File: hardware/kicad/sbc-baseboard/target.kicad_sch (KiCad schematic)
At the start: 59 parts, among them J11 Relay COM/NO/NC, J12 Relay COM/NO/NC, J13 Console VREF/TXD/RXD/GND, J14 +5V_TGT out, J15 GPIO + I2C breakout, J18 PSU in (isolated), J19 PSU out (isolated), K701 G6K-2F-Y DC5, K702 G6K-2F-Y DC5, K703 JW1FSN-DC5V, Q701 2N7002, Q702 2N7002, Q703 AO3400A, U701 TXB0104PW, U702 TXB0108PW, U703 TXS0102DCU, U704 TPS26630RGE, U705 LTV-817

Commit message: Re-lay out every sheet around its main component
Nets fan out of each hub IC as wires at pin pitch; connectors, series
parts, pull-ups and power symbols sit at the lane ends, and labels are
kept for nets that leave the page. Supply pins share a bus with their
decoupling; ESD arrays sit on the connector's D-/D+ rows and port
switches on the VBUS row, so every wire into a receptacle is straight;
the stacked USB-A is a two-unit symbol, one per port. Relays move to
their own sheet (8xx). ESD diodes use KiCad's PESD5V0S1UL in SOD-882.

Generator: gen/fanout.py (lane engine), gen/check_geom.py (endpoint
contacts), gen/netcheck.py (wire-level rail merges). ERC, both checks
and a renumbering-tolerant netlist diff against the first pass all
clean; 331 parts, 354 nets.

Co-Authored-By: Claude Fable 5.1 <noreply@anthropic.com>
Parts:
- removed D701, D702: PESD5V0S1UL, Diode_SMD:D_SOD-523, symbol Device:D_TVS
- removed D703, D705, D708, D710: 1N4148W, Diode_SMD:D_SOD-123, symbol Diode:1N4148W
- removed D704, D706, D709: LED RED, LED_SMD:LED_0603_1608Metric, symbol Device:LED
- removed D707: LED GREEN, LED_SMD:LED_0603_1608Metric, symbol Device:LED
- removed J11, J12: Relay COM/NO/NC, Connector_Phoenix_MC:PhoenixContact_MC_1,5_3-G-3.5_1x03_P3.50mm_Horizontal, symbol Connector_Generic:Conn_01x03
- removed J18: PSU in (isolated), Connector_Phoenix_MSTB:PhoenixContact_MSTBA_2,5_2-G-5,08_1x02_P5.08mm_Horizontal, symbol Connector_Generic:Conn_01x02
- removed J19: PSU out (isolated), Connector_Phoenix_MSTB:PhoenixContact_MSTBA_2,5_2-G-5,08_1x02_P5.08mm_Horizontal, symbol Connector_Generic:Conn_01x02
- removed K701, K702: G6K-2F-Y DC5, Relay_SMD:Relay_DPDT_Omron_G6K-2F-Y, symbol Relay:G6K-2
- removed K703: JW1FSN-DC5V, Relay_THT:Relay_SPDT_Panasonic_JW1_FormC, symbol sbcbb:JW1FSN
- removed Q701, Q702: 2N7002, Package_TO_SOT_SMD:SOT-23, symbol Transistor_FET:2N7002
- removed Q703: AO3400A, Package_TO_SOT_SMD:SOT-23, symbol Transistor_FET:AO3400A
- removed R709: 75k, Resistor_SMD:R_0603_1608Metric, symbol Device:R
- removed R710: 3.65k 1%, Resistor_SMD:R_0603_1608Metric, symbol Device:R
- removed R711, R712, R720: 10k, Resistor_SMD:R_0603_1608Metric, symbol Device:R
- removed R713: 20k, Resistor_SMD:R_0603_1608Metric, symbol Device:R
- removed R714, R716: 1k, Resistor_SMD:R_0603_1608Metric, symbol Device:R
- removed R715: 2.2k, Resistor_SMD:R_0603_1608Metric, symbol Device:R
- removed R717: 100k, Resistor_SMD:R_0603_1608Metric, symbol Device:R
- removed R718, R719: 1.8k, Resistor_SMD:R_1206_3216Metric, symbol Device:R
- removed U705: LTV-817, Package_DIP:DIP-4_W7.62mm, symbol Isolator:LTV-817
- added C712: 10n, Capacitor_SMD:C_0603_1608Metric, symbol Device:C
- added D701, D702: PESD5V0S1UL, Diode_SMD:D_SOD-882, symbol Diode:PESD5V0S1UL
- added D703: LED GREEN, LED_SMD:LED_0603_1608Metric, symbol Device:LED
- C707: value 10n -> 100n
- C708: value 1n -> 100n
- C710: value 100n -> 22u; footprint Capacitor_SMD:C_0603_1608Metric -> Capacitor_SMD:C_1206_3216Metric
- C711: value 22u -> 1n; footprint Capacitor_SMD:C_1206_3216Metric -> Capacitor_SMD:C_0603_1608Metric
- R702: value 2.2k -> 75k
- R703: value 1k -> 196k
- R704: value 100k -> 10k
- R705: value 2.2k -> 1k
- R706: value 1k -> 10k
- R707: value 100k -> 20k
- R708: value 196k -> 3.65k 1%
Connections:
- net RLY2_DRV is gone; now on net +3V3: R706.1
- net +3V3: now also C703.2, C705.2, C707.2, R704.1; no longer C702.1, C704.1, C706.1
- net +5V_TGT: now also C708.1, R703.2; no longer C710.1, R708.1
- net GND: now also C702.1, C703.1, C704.1, C705.1, C706.1, C707.1, R702.2, R708.2, C712.2, D701.2 (A), D702.2 (A), D703.1 (K); no longer C702.2, C703.2, C704.2, C705.2, C706.2, C707.2, R704.2
- net TGT_EN: now also R704.2
- net TGT_FAULT_N: now also R706.2
- net TGT_IMON: now also C711.1, R707.1; no longer C708.1
- net VREF_TGT: now also C702.2, C704.2, C706.2; no longer C703.1, C705.1
- net at R705.2: now also D703.2 (A)
- net +5V_PORTS: no longer names the net of R705.1
- net +5V_PORTS: now also C710.1, J14.1 (Pin_1), U704.17 (OUT), U704.18 (OUT); no longer R702.1
- removed net +5V_TGT_OUT: C711.1, J14.1 (Pin_1), U704.17 (OUT), U704.18 (OUT)
- net J13_RXD: no longer names the net of J13.3 (Pin_3), U701.3 (A2)
- net J13_RXD: now also D702.1 (K)
- net J13_TXD: no longer names the net of J13.2 (Pin_2), U701.2 (A1)
- net J13_TXD: now also D701.1 (K)
- net RLY1_DRV: no longer names the net of R703.1
- net RLY1_DRV: now also R702.1, U704.6 (UVLO)
- removed net RLY1_GATE: R703.2, R704.1
- removed net RLY2_GATE: R706.2, R707.1
- net TGT_DVDT: no longer names the net of U704.9 (dVdT)
- net TGT_DVDT: now also C712.1; no longer C707.1
- net TGT_ILIM: no longer names the net of U704.10 (ILIM)
- net TGT_ILIM: now also R708.1
- removed net TGT_UVLO: R708.2, U704.6 (UVLO)
- no-connect marks 26 -> 19
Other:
- note added: "TPS26630: ILIM 3.65k -> ~5 A, UVLO 196k/75k -> 4.3 V, OVP/MODE/PGTH to GND (latch-off). IMON 20k -> 2.8 V at 5 A into PTB2."
- note removed: "IMON 20k -> 2.8 V at 5 A into K64 ADC (PTB2). SHDN = TGT_EN, pulled up: boots ON."
- note removed: "Internal 10k pull-ups on both sides; K64-side 4.7k pull-ups are on the MCU sheet."
- note removed: "K703 JW1FSN pad map COM=6 NO=4 NC=2: VERIFY against the Panasonic terminal drawing before fab."
- note removed: "Opto LED: 2x1.8k 1206 in series, 1 mA at 5 V, 8 mA / 0.12 W each at 30 V. D708 protects a reversed PSU."
- note removed: "PSU_PRESENT_N is active low at the K64. No LED on the passthrough itself."
- note removed: "Passthrough J18 -> K703 (NO) -> J19 on nets PSU_VP / PSU_VOUT / PSU_GND that touch no board net. Opto only."
- note removed: "Relays boot de-energized (gate pull-downs). K701/K702 G6K-2F-Y: pole 1 used (COM 3, NC 2, NO 4); pole 2 unused."
- note removed: "TPS26630: ILIM 3.65k -> ~5 A (3k = 6 A, 4.02k = 4.5 A). UVLO 196k/75k -> 4.3 V. OVP/MODE/PGTH to GND (defaults, latch-off)."
- title: Target I/O: console, GPIO+I2C, relays, +5V_TGT eFuse, PSU passthrough -> Target I/O: console, GPIO + I2C breakout, +5V_TGT eFuse

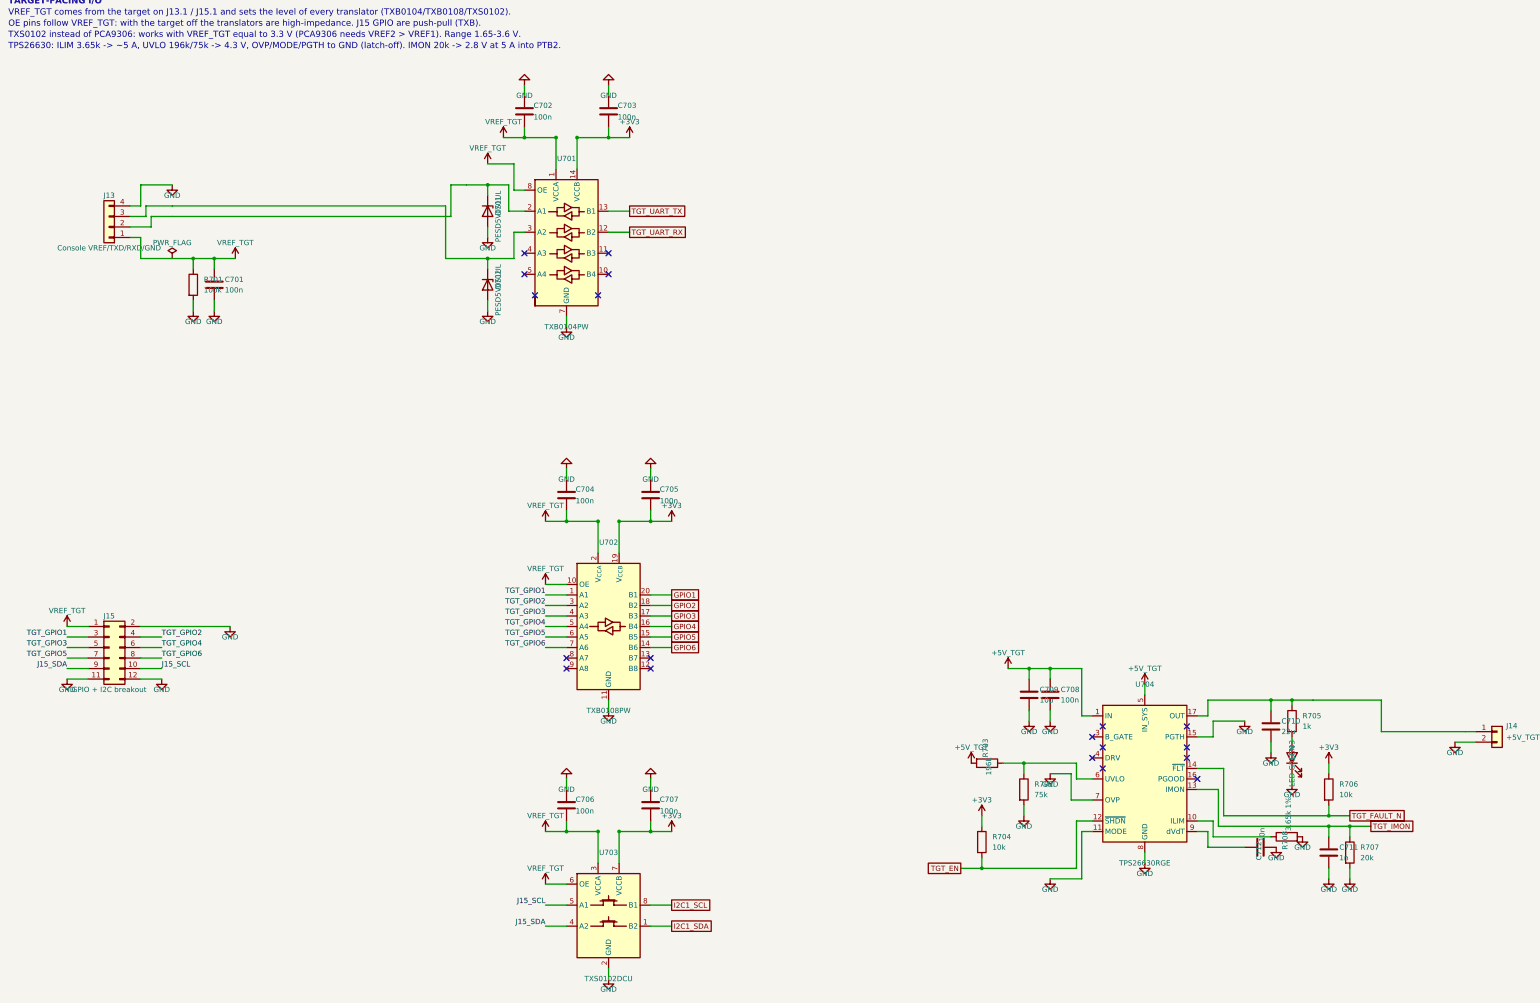
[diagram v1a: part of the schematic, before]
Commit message: Symbol direction, field text and decoupling ladders across every sheet
Every GND symbol now hangs down and every rail stands up: decoupling
hangs from the supply bus into a GND rail with one GND symbol at the end
(ladders), rails on crowded supply pins are jogged sideways, the SWD
header is mirrored instead of rotated. Field text on in-line parts reads
horizontally (KiCad adds the symbol rotation to the field angle) and is
placed by lane direction; hanging parts carry their text on the side away
from the pin; IC reference and value sit where the library put them.
Power sheet: bus buffer moved under the STUSB4500's I2C lanes with direct
routes, programmer by label, buck drawn as a box with its input and
output capacitors as ladders. New gen/check_layout.py reports text and
wire overlaps and wrong-way power symbols; PDF export draws hop-overs.

ERC 0, no merged rails, netlist equivalent; text-overlap residue listed
in the layout checker output remains on the hub, relays and DAPLink.

Co-Authored-By: Claude Fable 5.1 <noreply@anthropic.com>
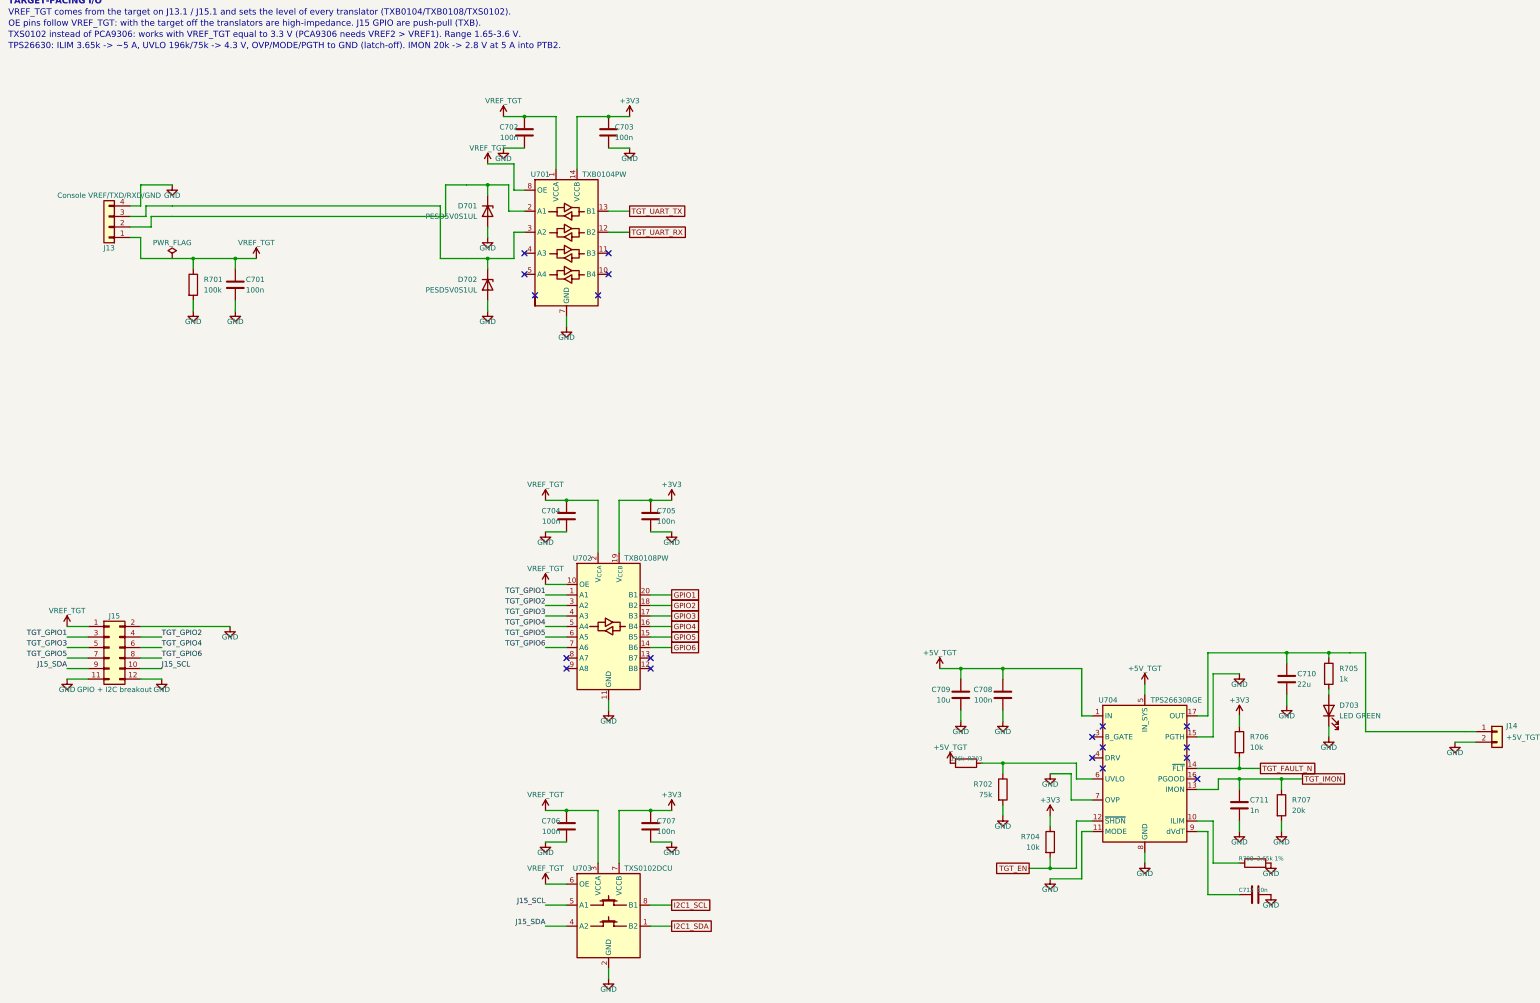
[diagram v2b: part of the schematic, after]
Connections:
- net +3V3: now also C703.1, C705.1, C707.1; no longer C703.2, C705.2, C707.2
- net GND: now also C702.2, C703.2, C704.2, C705.2, C706.2, C707.2; no longer C702.1, C703.1, C704.1, C705.1, C706.1, C707.1
- net VREF_TGT: now also C702.1, C704.1, C706.1; no longer C702.2, C704.2, C706.2

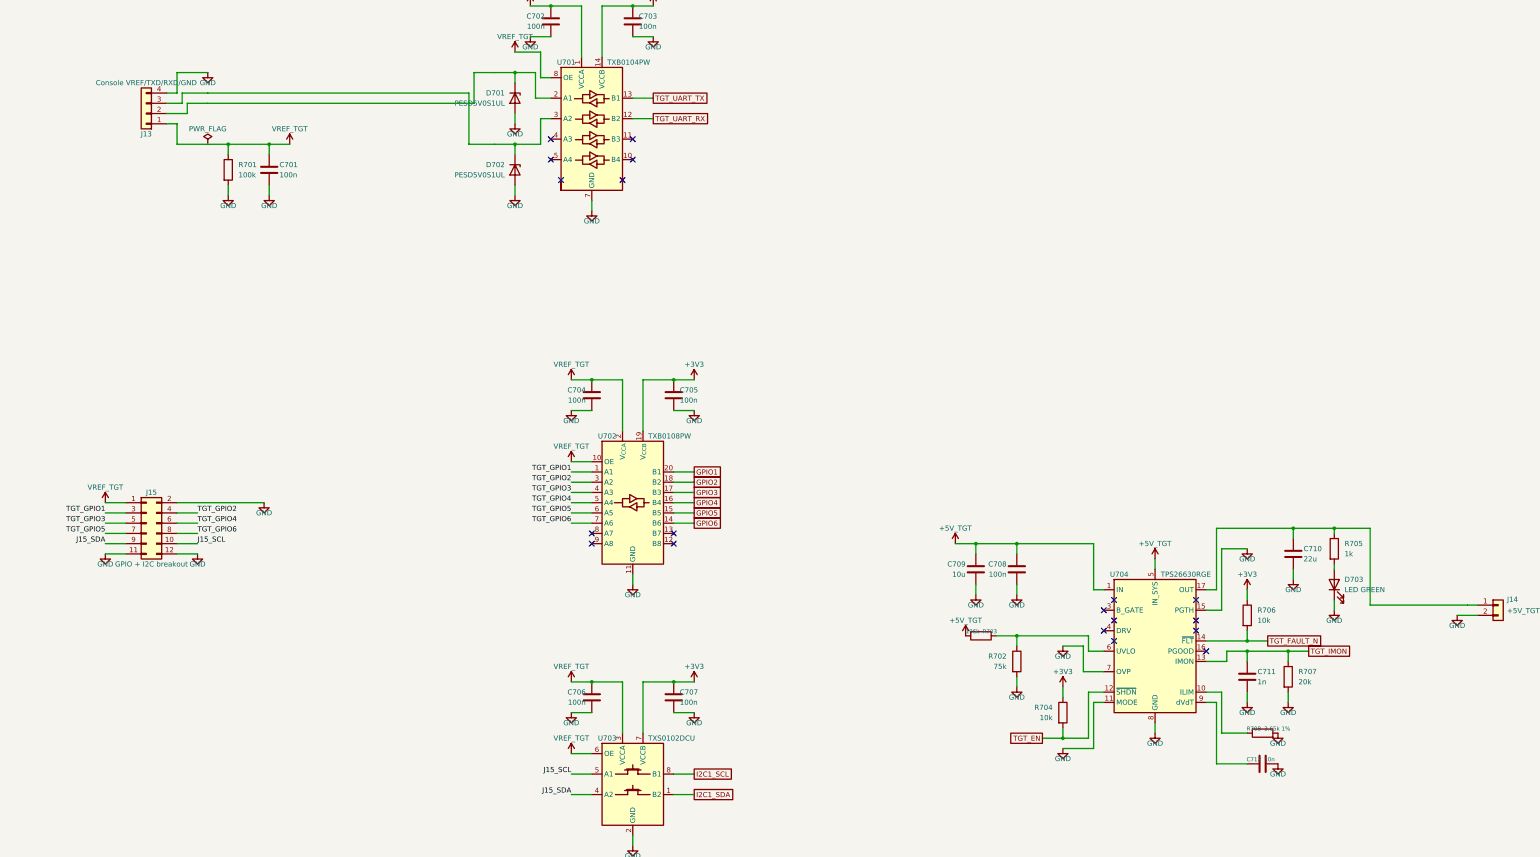
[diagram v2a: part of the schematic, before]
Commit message: Placement pass: every sheet clean on all four layout gates
Hanging parts now sit with their near pin between rows, so a pull-up on
the next lane crosses only its lead; parts slide past a neighbour's parts
and text, not its plain wire, and never let a wire run through a body or
a rail symbol. Chains on top/bottom pins run sideways first. Route
channels are numbered per route. Power symbols that would land on a
neighbouring wire get a jog or a hook. The VBUS sense divider moved to
the K64's ADC pin so J3's VBUS lane is a short stretch the ESD array taps;
the J1 tap sits before its divider. Relay coil clusters are drawn by the
engine. Port switches moved so OUT stays on the VBUS row.

ERC 0, no endpoint contacts, no merged rails, no wires through bodies,
no inverted power symbols, on all eight sheets; netlist equivalent to the
first pass (331 parts, 354 nets); USB D+/D-, VBUS and I2C paths verified
pin by pin.

Co-Authored-By: Claude Fable 5.1 <noreply@anthropic.com>
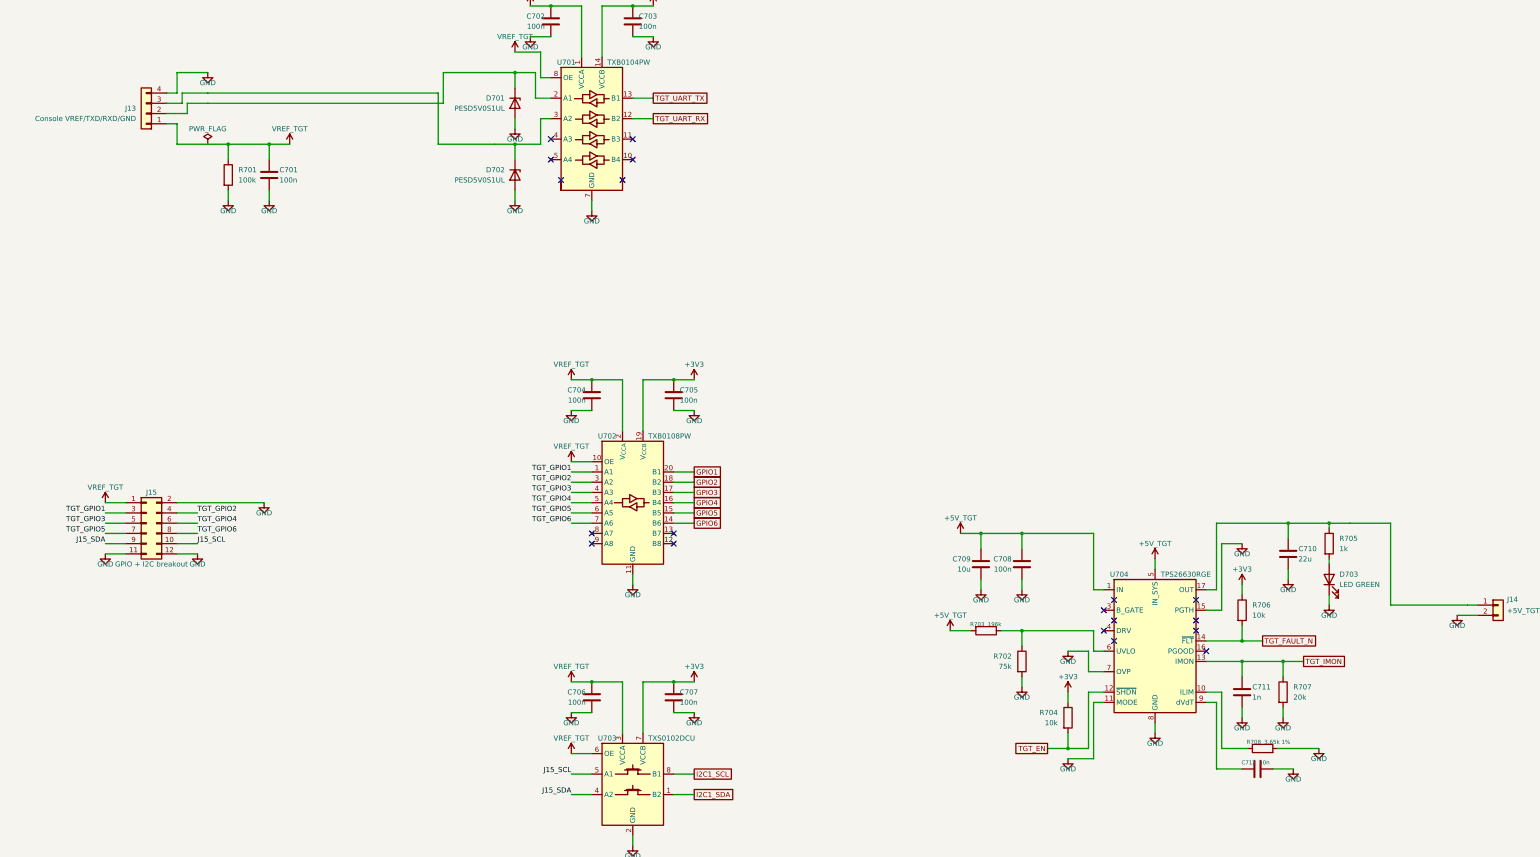
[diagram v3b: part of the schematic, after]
